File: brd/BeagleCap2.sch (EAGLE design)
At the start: 35 parts, among them IC2 7805TV, J2 DS18B20, J3 Battery, U1 DHT22, X1 Conn BNC : pH, X2 Conn BNC : Dissolved Oxygen, X3 Conn BNC : Conductivity, X4 Conn BNC : ORP

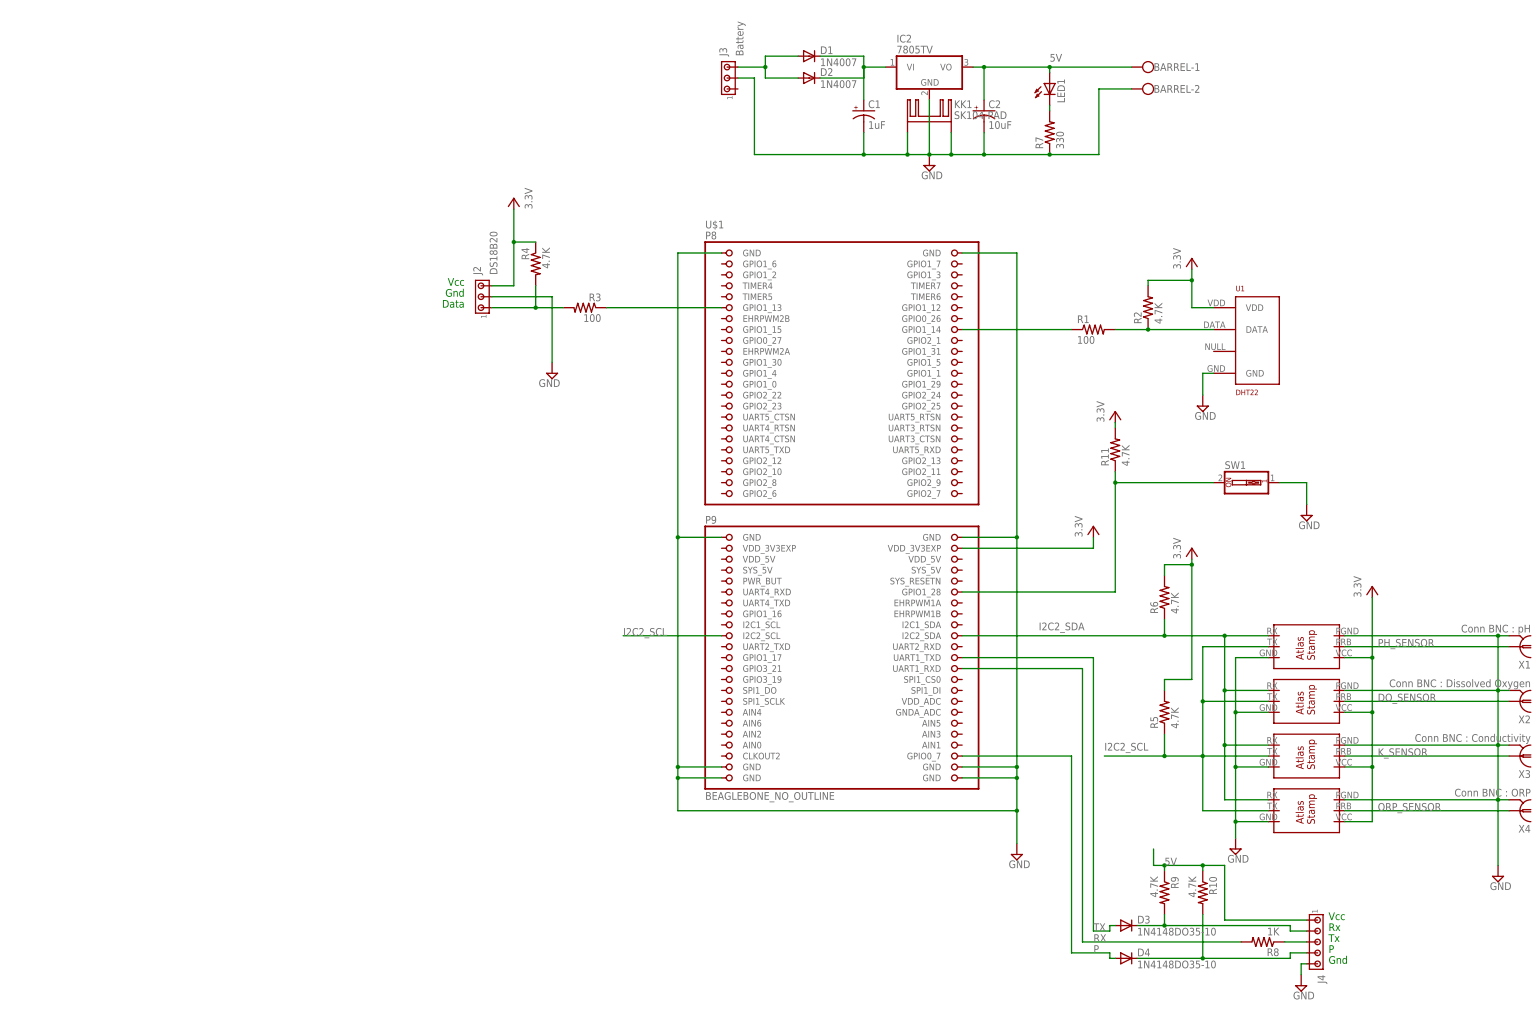
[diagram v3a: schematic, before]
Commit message: Updated schematic
Added:
RTC
Logic for power management
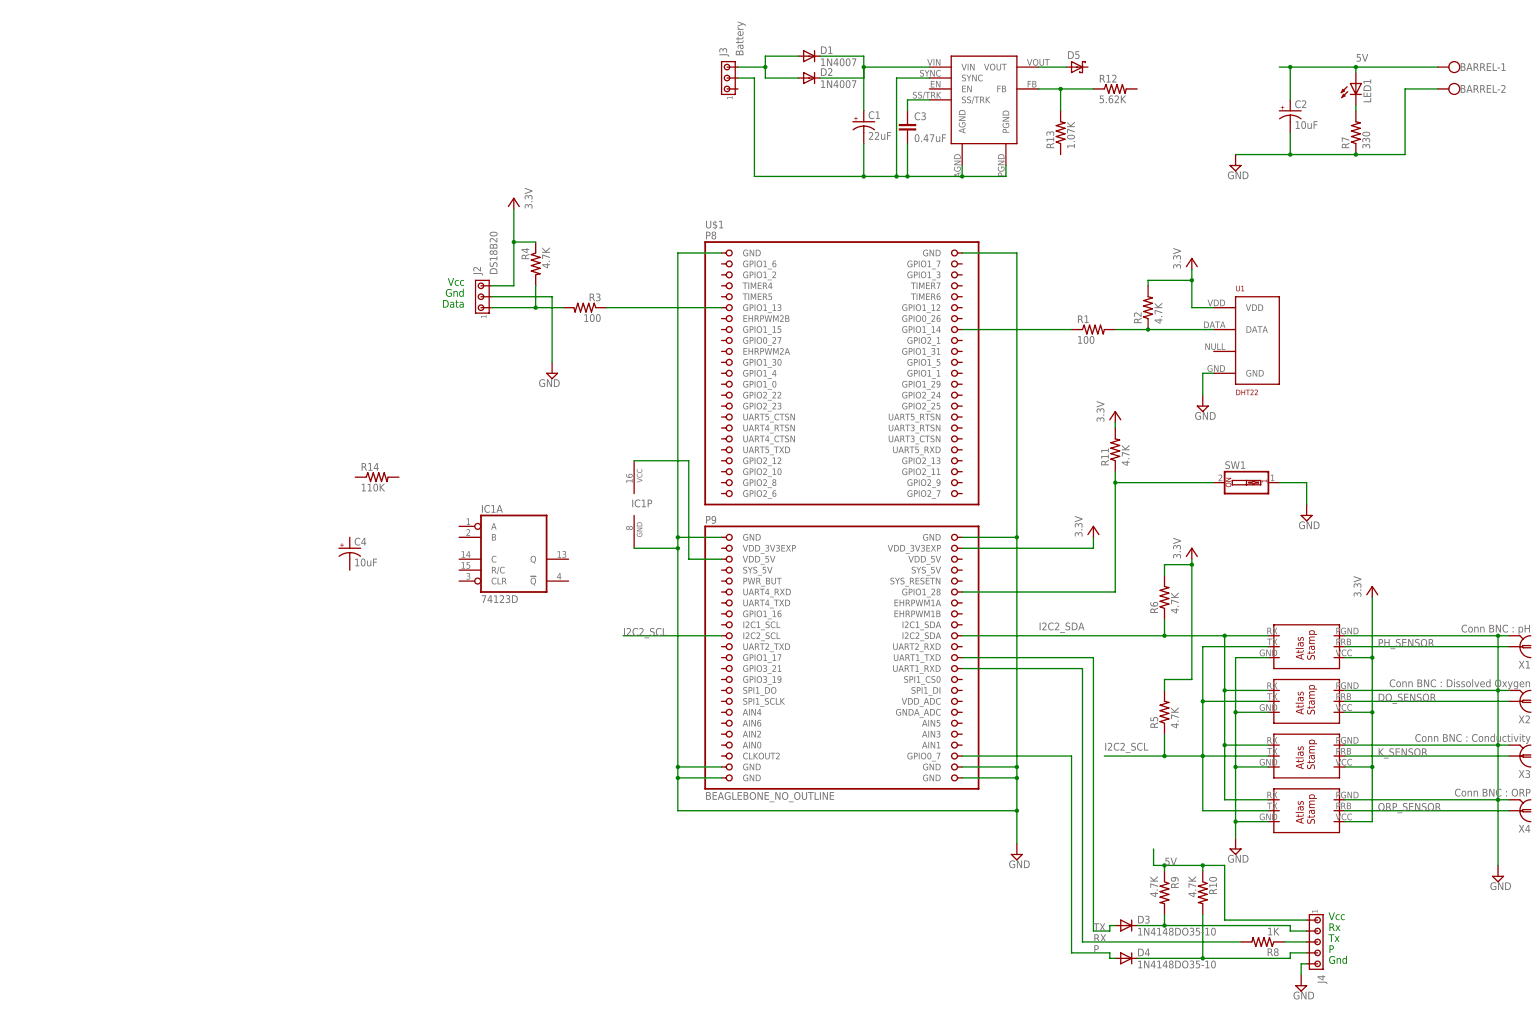
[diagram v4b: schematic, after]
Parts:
- removed IC2: 7805TV, linear:7805TV
- removed KK1: SK104-PAD, heatsink:SK104-PAD
- added C3: 0.47uF, capacitor-wima:C5/3
- added C4: 10uF, rcl:CPOL-USE2-5
- added D5: (no value), diode:SCHOTTKY-DIODEC4111-15
- added IC1: 74123D, 74xx-us:74123D
- added R12: 5.62K, resistor:R-US_R0805
- added R13: 1.07K, resistor:R-US_R0805
- added R14: 110K, adafruit:R-US_R0805
- added U$6: LMZ23605, Aquarius:LMZ23605
- C1: value 1uF -> 22uF
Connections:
- new net AGND: C1.-, C3.2, J3.2, U$6.AGND, U$6.PGND, U$6.SYNC
- new net N$13: R12.1, R13.2, U$6.FB
- new net N$14: C3.1, U$6.SS/TRK
- new net VOUT: D5.A, U$6.VOUT
- net 5V: now also IC1P.VCC, U$1.VDD_5V@1; no longer IC2.VO
- net GND: now also IC1P.GND; no longer C1.-, IC2.GND, J3.2, KK1.K@1, KK1.K@2
- net VIN: now also U$6.VIN; no longer IC2.VI
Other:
- moved on the sheet: BARREL-1, BARREL-2, C1, C2, LED1, R7

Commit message: Modification au makefile du DHT22 et autre modifs
Sur le board
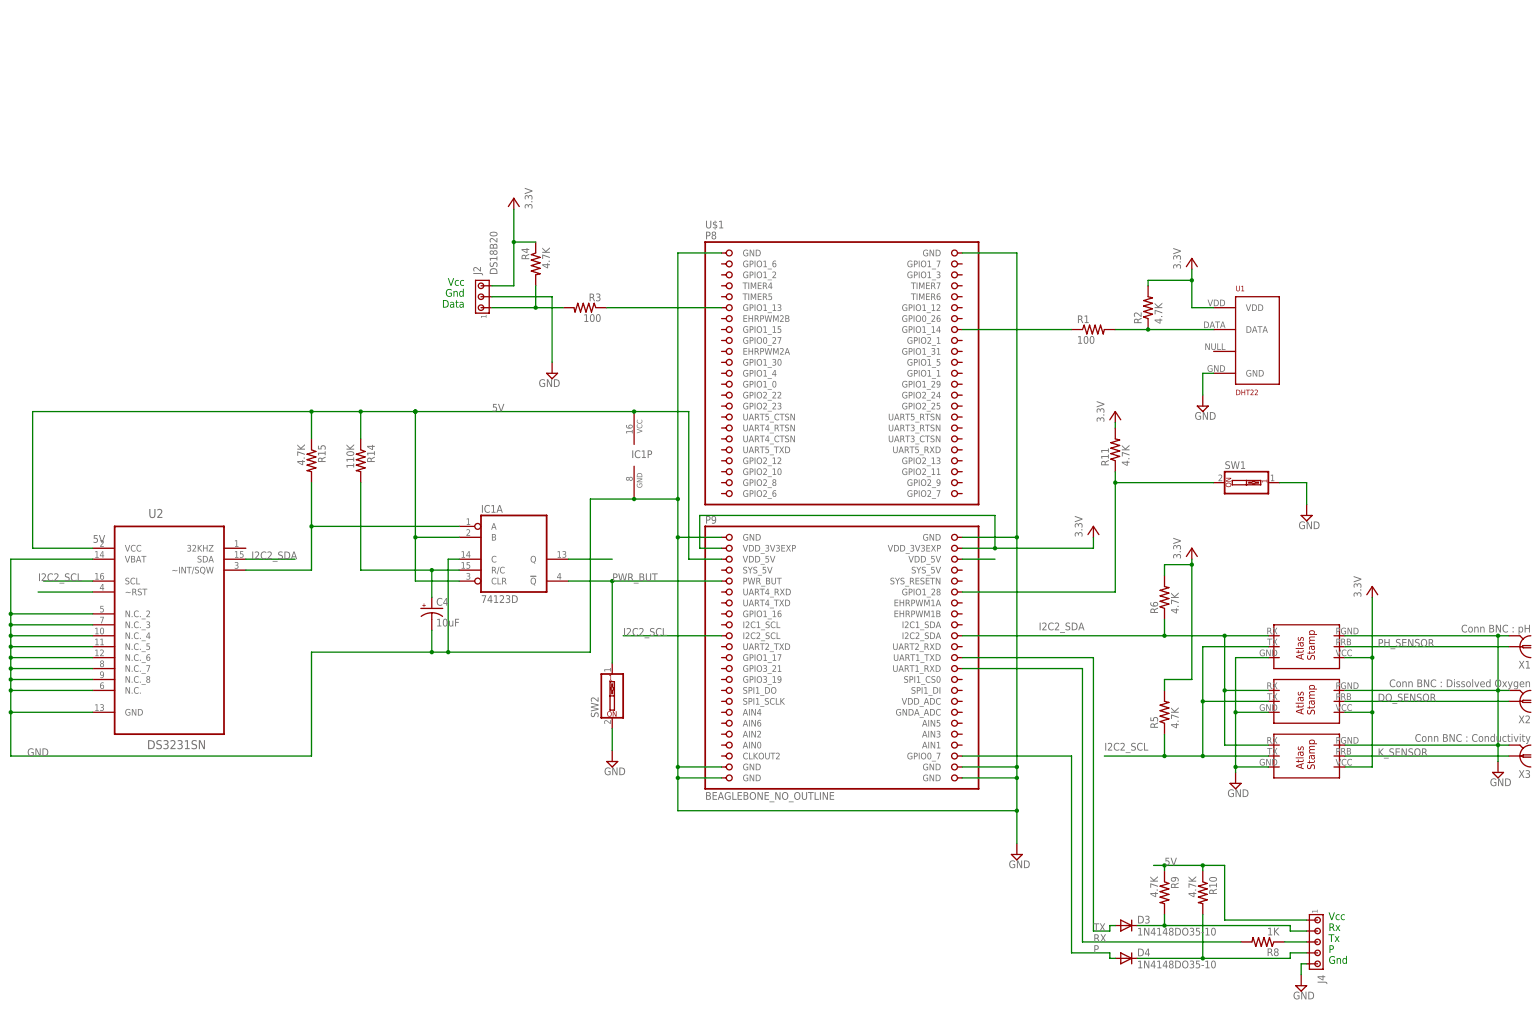
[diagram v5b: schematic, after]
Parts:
- removed BARREL: (no value), con-wago-500:W237-102
- removed C1: 22uF, rcl:CPOL-USE2-5
- removed C2: 10uF, rcl:CPOL-USE2-5
- removed C3: 0.47uF, capacitor-wima:C5/3
- removed D1, D2: 1N4007, diode:1N4004
- removed D5: (no value), diode:SCHOTTKY-DIODEC4111-15
- removed J3: Battery, con-amp:MTA03-100
- removed LED1: (no value), led:LEDSML0805
- removed R12: 5.62K, resistor:R-US_R0805
- removed R13: 1.07K, resistor:R-US_R0805
- removed R7: 330, adafruit:R-US_R0805
- removed U$5: ATLAS_STAMP, LEDscape:ATLAS_STAMP
- removed U$6: LMZ23605, Aquarius:LMZ23605
- removed X4: Conn BNC : ORP, con-coax:1-227161-0
- added R15: 4.7K, adafruit:R-US_R0805
- added SW2: (no value), special:SW_DIP-1
- added U2: DS3231SN, Maxim_By_element14_Batch_1:DS3231SN
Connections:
- removed net AGND: C1.-, C3.2, J3.2, U$6.AGND, U$6.PGND, U$6.SYNC
- removed net N$13: R12.1, R13.2, U$6.FB
- removed net N$14: C3.1, U$6.SS/TRK
- removed net N$2: LED1.C, R7.2
- removed net ORP_SENSOR: U$5.PRB, X4.1
- removed net VIN: C1.+, D1.C, D2.C, U$6.VIN
- removed net VOUT: D5.A, U$6.VOUT
- new net INT: IC1A.A, R15.2, U2.~INT/SQW
- new net N$12: U2.~RST
- new net N$17: C4.+, IC1A.R/C, R14.2
- new net N$20: IC1A.Q
- new net PWR_BUT: IC1A.!Q, SW2.1, U$1.PWR_BUT
- net 3.3V: now also U$1.VDD_3V3EXP@1; no longer U$5.VCC
- net 5V: now also IC1A.B, IC1A.CLR, R14.1, R15.1, U2.VCC; no longer BARREL-1.KL, C2.+, LED1.A
- net GND: now also C4.-, IC1A.C, SW2.2, U2.GND, U2.N.C., U2.N.C._2, U2.N.C._3, U2.N.C._4, U2.N.C._5, U2.N.C._6, U2.N.C._7, U2.N.C._8, U2.VBAT; no longer BARREL-2.KL, C2.-, R7.1, U$5.GND, U$5.PGND, X4.2
- net I2C2_SCL: now also U2.SCL; no longer U$5.TX
- net I2C2_SDA: now also U2.SDA; no longer U$5.RX
- net N$1: now also U$1.VDD_5V@2; no longer D1.A, D2.A, J3.3
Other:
- moved on the sheet: C4, IC1P, R14
